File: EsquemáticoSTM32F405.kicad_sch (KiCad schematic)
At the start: 24 parts, among them SW3 XDTD-0304-215, U13 Green LED, U4 STM32F405RGT6, X1 32.768kHz 7pF SMD, X2 8Mhz 10pF

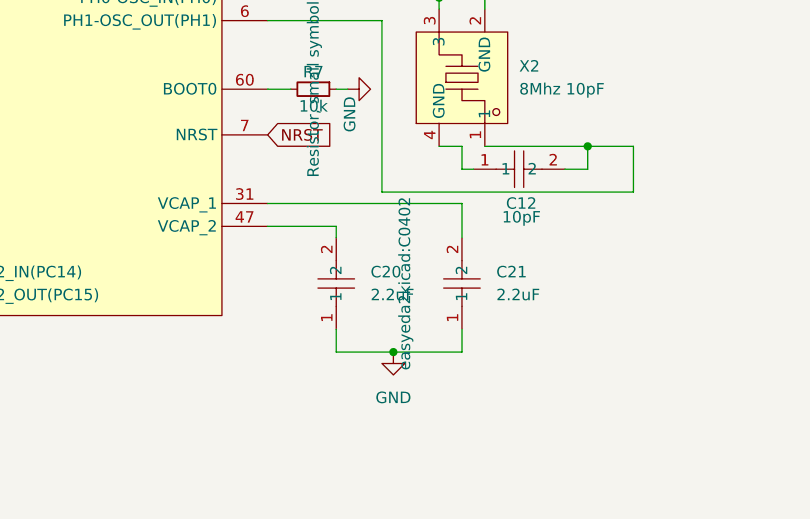
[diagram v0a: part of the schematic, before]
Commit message: Footprints V2
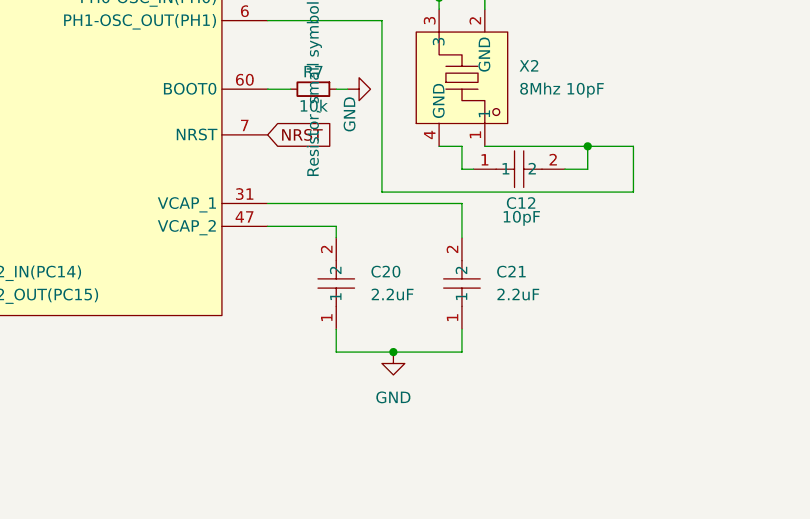
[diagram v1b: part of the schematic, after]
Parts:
- C20, C21, C23: footprint easyeda2kicad:C0402 -> Capacitor_SMD:C_0402_1005Metric_Pad0.74x0.62mm_HandSolder
- X1: footprint easyeda2kicad:FC-12M_L2.0-W1.2 -> Crystal:Crystal_SMD_2012-2Pin_2.0x1.2mm_HandSoldering
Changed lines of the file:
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@@
 			)
 		)
-		(property "Footprint" "easyeda2kicad:FC-12M_L2.0-W1.2"
+		(property "Footprint" "Crystal:Crystal_SMD_2012-2Pin_2.0x1.2mm_HandSoldering"
 			(at 273.05 220.98 0)
 			(hide yes)
@@
 			)
 		)
-		(property "Footprint" "easyeda2kicad:C0402"
+		(property "Footprint" "Capacitor_SMD:C_0402_1005Metric_Pad0.74x0.62mm_HandSolder"
 			(at 363.22 218.44 0)
 			(hide yes)
@@
 			)
 		)
-		(property "Footprint" "easyeda2kicad:C0402"
+		(property "Footprint" "Capacitor_SMD:C_0402_1005Metric_Pad0.74x0.62mm_HandSolder"
 			(at 273.05 209.55 0)
 			(hide yes)
@@
 			)
 		)
-		(property "Footprint" "easyeda2kicad:C0402"
+		(property "Footprint" "Capacitor_SMD:C_0402_1005Metric_Pad0.74x0.62mm_HandSolder"
 			(at 349.25 218.44 0)
+			(hide yes)
 			(show_name no)
 			(do_not_autoplace no)

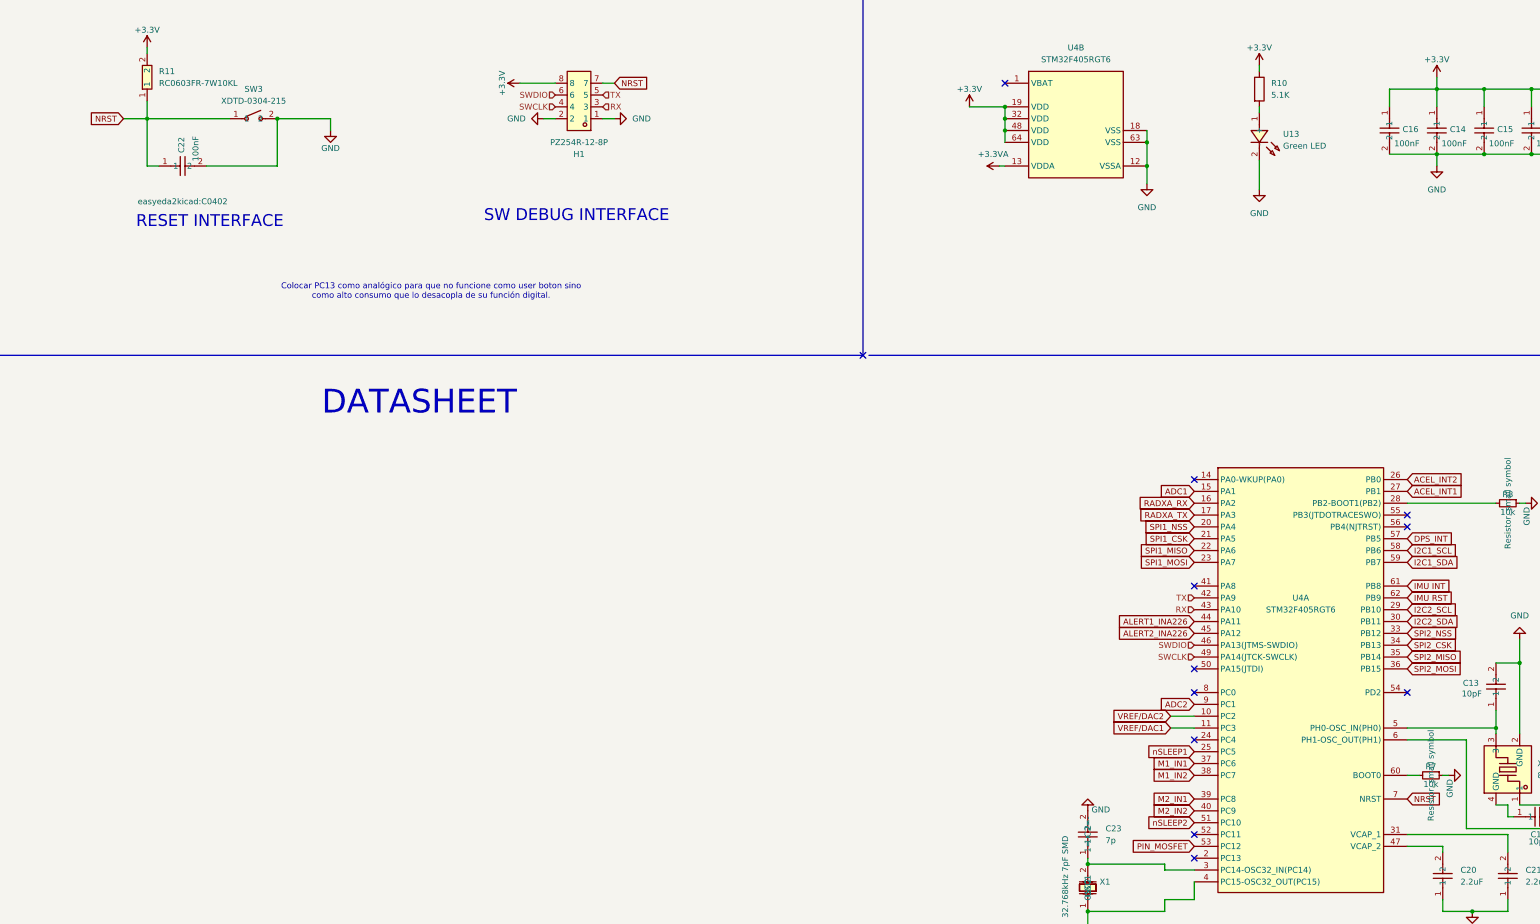
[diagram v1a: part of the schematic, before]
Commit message: Actualización de nets
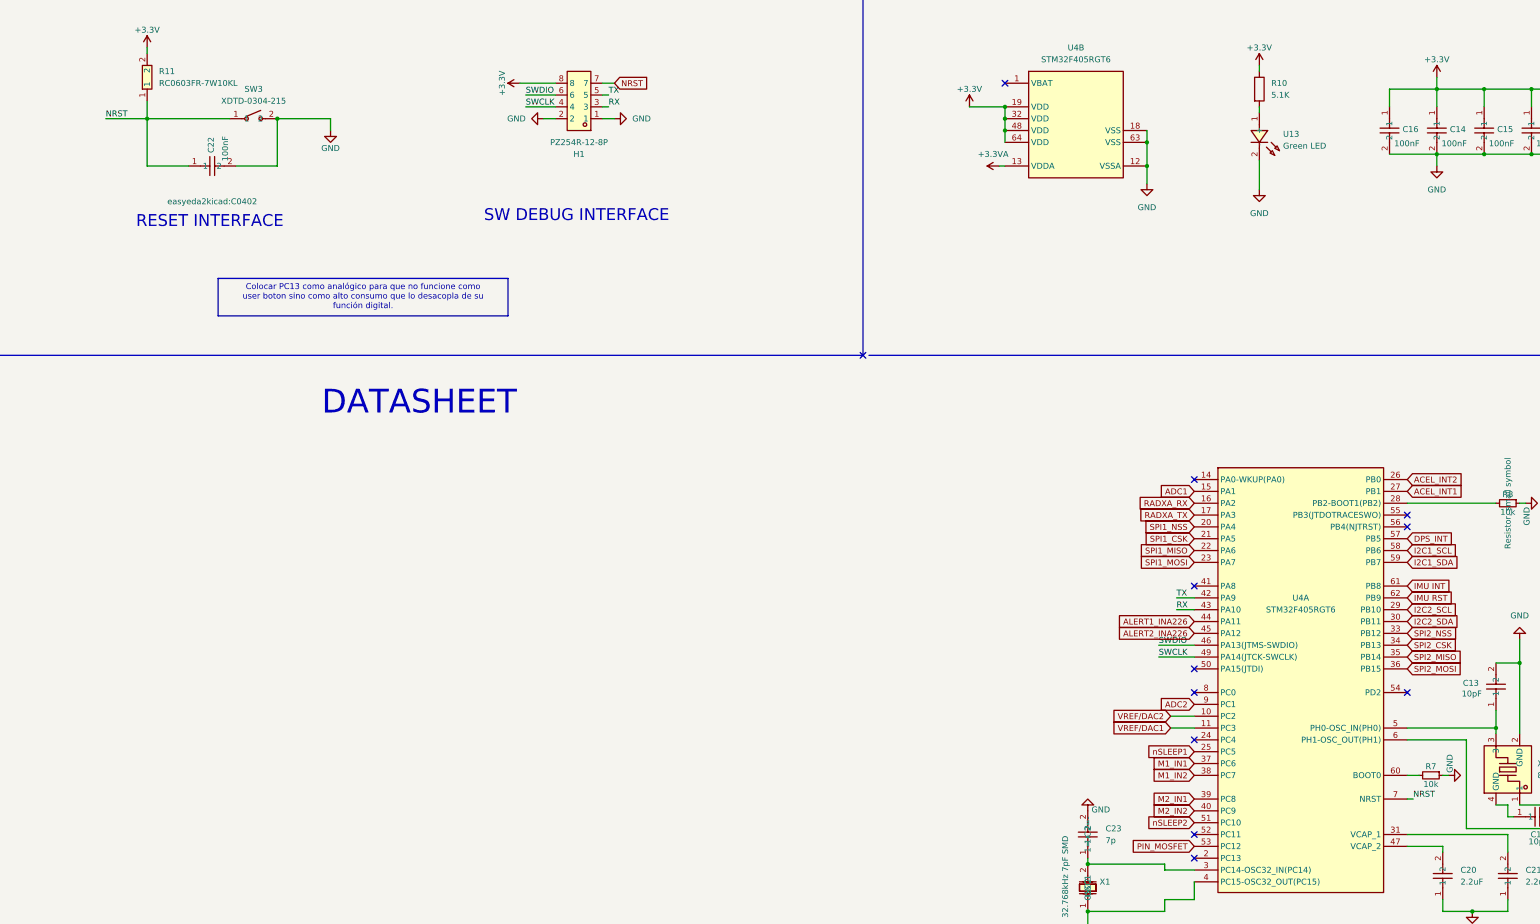
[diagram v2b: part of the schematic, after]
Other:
- note removed: "Colocar PC13 como analógico para que no funcione como user boton sino como alto consumo que lo desacopla de su función digital."
- moved on the sheet: C22

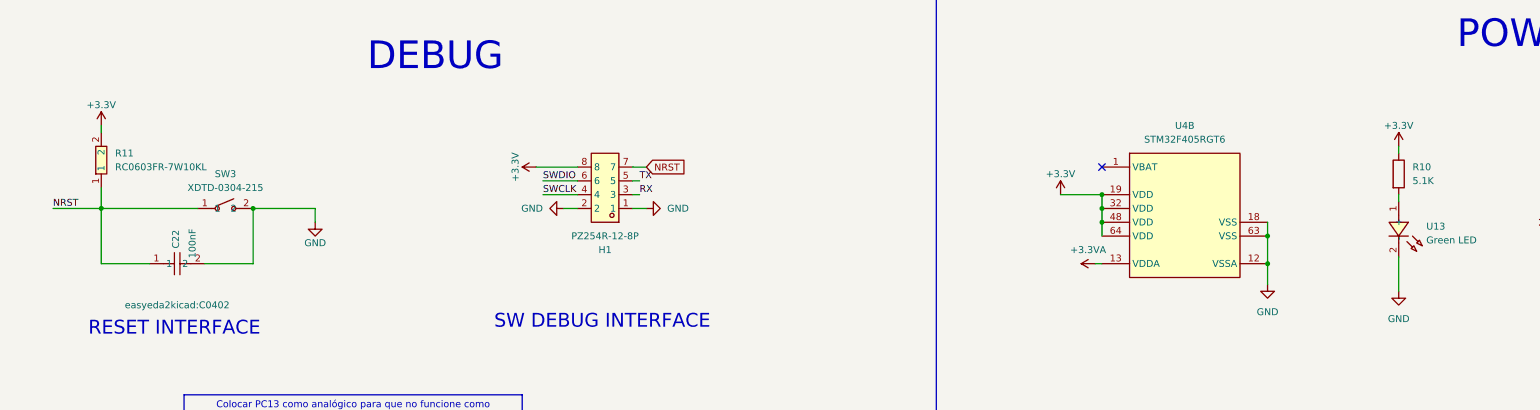
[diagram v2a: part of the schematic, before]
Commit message: Cantidad de errores en la PCB: 29
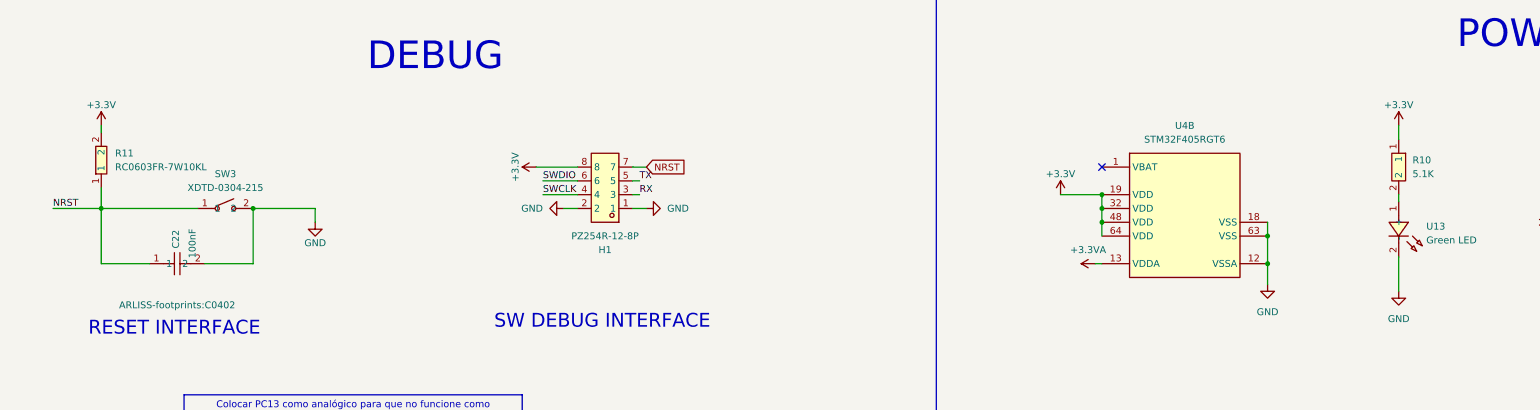
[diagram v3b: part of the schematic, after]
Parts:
- removed R10: 5.1K, symbol Device:R
- added R10: 5.1K, Resistor_SMD:R_0402_1005Metric_Pad0.72x0.64mm_HandSolder, symbol CANSAT_STM32_symbols:FRC0402F5101TS
- C11, C12, C13, C14, C15, C16, C17, C19, C22: footprint easyeda2kicad:C0402 -> ARLISS-footprints:C0402
- L3: footprint easyeda2kicad:L0402 -> ARLISS-footprints:L0402
- SW3: footprint easyeda2kicad:SW-SMD_L3.9-W3.0-P4.45 -> ARLISS-footprints:SW-SMD_L3.9-W3.0-P4.45
- U4: footprint easyeda2kicad:LQFP-64_L10.0-W10.0-P0.50-LS12.0-BL -> ARLISS-footprints:LQFP-64_L10.0-W10.0-P0.50-LS12.0-BL
- X2: footprint easyeda2kicad:CRYSTAL-SMD_4P-L3.2-W2.5-BL -> ARLISS-footprints:CRYSTAL-SMD_4P-L3.2-W2.5-BL
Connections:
- net +3.3V: now also R10.1
- net at U13.1 (+): now also R10.2
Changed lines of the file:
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@@
 	(wire
 		(pts
-			(xy 302.26 44.45) (xy 302.26 45.72)
+			(xy 302.26 40.64) (xy 302.26 43.18)
 		)
 		(stroke
@@
 			)
 		)
-		(property "Footprint" "easyeda2kicad:C0402"
+		(property "Footprint" "ARLISS-footprints:C0402"
 			(at 342.9 58.42 0)
 			(hide yes)
@@
 			)
 		)
-		(property "Footprint" "easyeda2kicad:C0402"
+		(property "Footprint" "ARLISS-footprints:C0402"
 			(at 361.95 213.36 0)
 			(hide yes)
@@
 	)
 	(symbol
+		(lib_id "CANSAT_STM32_symbols:FRC0402F5101TS")
+		(at 302.26 48.26 270)
+		(unit 1)
+		(body_style 1)
+		(exclude_from_sim no)
+		(in_bom yes)
+		(on_board yes)
+		(in_pos_files yes)
+		(dnp no)
+		(fields_autoplaced yes)
+		(property "Reference" "R10"
+			(at 304.8 46.9899 90)
+			(show_name no)
+			(do_not_autoplace no)
+			(effects
+				(font
+					(size 1.27 1.27)
+				)
+				(justify left)
+			)
+		)
+		(property "Value" "5.1K"
+			(at 304.8 49.5299 90)
+			(show_name no)
+			(do_not_autoplace no)
+			(effects
+				(font
+					(size 1.27 1.27)
+				)
+				(justify left)
+			)
+		)
+		(property "Footprint" "Resistor_SMD:R_0402_1005Metric_Pad0.72x0.64mm_HandSolder"
+			(at 294.64 48.26 0)
+			(hide yes)
+			(show_name no)
+			(do_not_autoplace no)
+			(effects
+				(font
+					(size 1.27 1.27)
+				)
+			)
+		)
+		(property "Datasheet" "https://www.lcsc.com/datasheet/C2906874.pdf"
+			(at 292.1 48.26 0)
+			(hide yes)
+			(show_name no)
+			(do_not_autoplace no)
+			(effects
+				(font
+					(size 1.27 1.27)
+				)
+			)
+		)
+		(property "Description" ""
+			(at 302.26 48.26 0)
+			(hide yes)
+			(show_name no)
+			(do_not_autoplace no)
+			(effects
+				(font
+					(size 1.27 1.27)
+				)
+			)
+		)
+		(property "Manufacturer" "FOJAN(富捷)"
+			(at 289.56 48.26 0)
+			(hide yes)
+			(show_name no)
+			(do_not_autoplace no)
+			(effects
+				(font
+					(size 1.27 1.27)
+				)
+			)
+		)
+		(property "MPN" "FRC0402F5101TS"
+			(at 287.02 48.26 0)
+			(hide yes)
+			(show_name no)
+			(do_not_autoplace no)
+			(effects
+				(font
+					(size 1.27 1.27)
+				)
+			)
+		)
+		(property "LCSC Part" "C2906874"
+			(at 284.48 48.26 0)
+			(hide yes)
+			(show_name no)
+			(do_not_autoplace no)
+			(effects
+				(font
+					(size 1.27 1.27)
+				)
+			)
+		)
+		(pin "1"
+		)
+		(pin "2"
+		)
+		(instances
+			(project "ARLISS_STM32_2026"
+				(path "/9719ea46-14c4-4409-9c57-49dd5454c03f/55efcca8-1297-47b0-ad35-b3f1b6f19299"
+					(reference "R10")
+					(unit 1)
+				)
+			)
+		)
+	)
+	(symbol
 		(lib_id "Device:R_Small")
 		(at 355.6 138.43 270)
@@
 			)
 		)
-		(property "Footprint" "easyeda2kicad:C0402"
+		(property "Footprint" "ARLISS-footprints:C0402"
 			(at 401.32 57.15 0)
 			(hide yes)
@@
 			)
 		)
-		(property "Footprint" "easyeda2kicad:C0402"
+		(property "Footprint" "ARLISS-footprints:C0402"
 			(at 322.58 58.42 0)
 			(hide yes)
@@
 			)
 		)
-		(property "Footprint" "easyeda2kicad:C0402"
+		(property "Footprint" "ARLISS-footprints:C0402"
 			(at 77.47 73.66 0)
 			(show_name no)
@@
 			)
 		)
-		(property "Footprint" "easyeda2kicad:C0402"
+		(property "Footprint" "ARLISS-footprints:C0402"
 			(at 332.74 58.42 0)
 			(hide yes)
@@
 	)
 	(symbol
-		(lib_id "Device:R")
-		(at 302.26 49.53 0)
-		(unit 1)
-		(body_style 1)
-		(exclude_from_sim no)
-		(in_bom yes)
-		(on_board yes)
-		(in_pos_files yes)
-		(dnp no)
-		(fields_autoplaced yes)
-		(property "Reference" "R10"
-			(at 304.8 48.2599 0)
-			(show_name no)
-			(do_not_autoplace no)
-			(effects
-				(font
-					(size 1.27 1.27)
-				)
-				(justify left)
-			)
-		)
-		(property "Value" "5.1K"
-			(at 304.8 50.7999 0)
-			(show_name no)
-			(do_not_autoplace no)
-			(effects
-				(font
-					(size 1.27 1.27)
-				)
-				(justify left)
-			)
-		)
-		(property "Footprint" ""
-			(at 300.482 49.53 90)
-			(hide yes)
-			(show_name no)
-			(do_not_autoplace no)
-			(effects
-				(font
-					(size 1.27 1.27)
-				)
-			)
-		)
-		(property "Datasheet" ""
-			(at 302.26 49.53 0)
-			(hide yes)
-			(show_name no)
-			(do_not_autoplace no)
-			(effects
-				(font
-					(size 1.27 1.27)
-				)
-			)
-		)
-		(property "Description" "Resistor"
-			(at 302.26 49.53 0)
-			(hide yes)
-			(show_name no)
-			(do_not_autoplace no)
-			(effects
-				(font
-					(size 1.27 1.27)
-				)
-			)
-		)
-		(pin "2"
-		)
-		(pin "1"
-		)
-		(instances
-			(project "ARLISS_STM32_2026"
-				(path "/9719ea46-14c4-4409-9c57-49dd5454c03f/55efcca8-1297-47b0-ad35-b3f1b6f19299"
-					(reference "R10")
-					(unit 1)
-				)
-			)
-		)
-	)
-	(symbol
 		(lib_id "CANSAT_STM32_symbols:GRM155Z71A225KE44D")
 		(at 355.6 218.44 90)
@@
 			)
 		)
-		(property "Footprint" "easyeda2kicad:LQFP-64_L10.0-W10.0-P0.50-LS12.0-BL"
+		(property "Footprint" "ARLISS-footprints:LQFP-64_L10.0-W10.0-P0.50-LS12.0-BL"
 			(at 311.15 227.33 0)
 			(hide yes)
@@
 			)
 		)
-		(property "Footprint" "easyeda2kicad:LQFP-64_L10.0-W10.0-P0.50-LS12.0-BL"
+		(property "Footprint" "ARLISS-footprints:LQFP-64_L10.0-W10.0-P0.50-LS12.0-BL"
 			(at 262.89 109.22 0)
 			(hide yes)
@@
 			)
 		)
-		(property "Footprint" "easyeda2kicad:C0402"
+		(property "Footprint" "ARLISS-footprints:C0402"
 			(at 273.05 234.95 0)
 			(hide yes)
@@
 	(symbol
 		(lib_id "power:+3.3V")
-		(at 302.26 44.45 0)
+		(at 302.26 40.64 0)
 		(unit 1)
 		(body_style 1)
@@
 		(dnp no)
 		(property "Reference" "#PWR095"
-			(at 302.26 48.26 0)
+			(at 302.26 44.45 0)
 			(hide yes)
 			(show_name no)
@@
 		)
 		(property "Value" "+3.3V"
-			(at 302.26 40.64 0)
+			(at 302.26 36.83 0)
 			(show_name no)
 			(do_not_autoplace no)
@@
 		)
 		(property "Footprint" ""
-			(at 302.26 44.45 0)
+			(at 302.26 40.64 0)
 			(hide yes)
 			(show_name no)
@@
 		)
 		(property "Datasheet" ""
-			(at 302.26 44.45 0)
+			(at 302.26 40.64 0)
 			(hide yes)
 			(show_name no)
@@
 		)
 		(property "Description" ""
-			(at 301.752 34.798 0)
+			(at 301.752 30.988 0)
 			(show_name no)
 			(do_not_autoplace no)
@@
 			)
 		)
-		(property "Footprint" "easyeda2kicad:L0402"
+		(property "Footprint" "ARLISS-footprints:L0402"
 			(at 370.84 57.15 0)
 			(hide yes)
@@
 			)
 		)
-		(property "Footprint" "easyeda2kicad:C0402"
+		(property "Footprint" "ARLISS-footprints:C0402"
 			(at 353.06 58.42 0)
 			(hide yes)
@@
 			)
 		)
-		(property "Footprint" "easyeda2kicad:CRYSTAL-SMD_4P-L3.2-W2.5-BL"
+		(property "Footprint" "ARLISS-footprints:CRYSTAL-SMD_4P-L3.2-W2.5-BL"
 			(at 365.76 195.58 0)
 			(hide yes)
@@
 			)
 		)
-		(property "Footprint" "easyeda2kicad:SW-SMD_L3.9-W3.0-P4.45"
+		(property "Footprint" "ARLISS-footprints:SW-SMD_L3.9-W3.0-P4.45"
 			(at 86.36 63.5 0)
 			(hide yes)
@@
 			)
 		)
-		(property "Footprint" "easyeda2kicad:C0402"
+		(property "Footprint" "ARLISS-footprints:C0402"
 			(at 360.68 177.8 0)
 			(hide yes)

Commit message: Cantidad de errores de la placa: 05
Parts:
- H1: footprint easyeda2kicad:HDR-TH_8P-P2.54-H-M-R2-C4-S2.54 -> ARLISS-footprints:HDR-TH_8P-P2.54-H-M-R2-C4-S2.54
- R11: footprint easyeda2kicad:R0603 -> ARLISS-footprints:R0603
- U13: footprint easyeda2kicad:LED0603-FD -> ARLISS-footprints:LED0603-FD
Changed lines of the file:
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@@
 			)
 		)
-		(property "Footprint" "easyeda2kicad:R0603"
+		(property "Footprint" "ARLISS-footprints:R0603"
 			(at 71.12 46.99 0)
 			(hide yes)
@@
 			)
 		)
-		(property "Footprint" "easyeda2kicad:LED0603-FD"
+		(property "Footprint" "ARLISS-footprints:LED0603-FD"
 			(at 294.64 59.69 0)
 			(hide yes)
@@
 			)
 		)
-		(property "Footprint" "easyeda2kicad:HDR-TH_8P-P2.54-H-M-R2-C4-S2.54"
+		(property "Footprint" "ARLISS-footprints:HDR-TH_8P-P2.54-H-M-R2-C4-S2.54"
 			(at 156.21 40.64 0)
 			(hide yes)
